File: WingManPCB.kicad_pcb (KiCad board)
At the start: 2 copper layers, 32 parts, among them SW1 SW_Push, U1 ATmega32U4-AU, Y1 Crystal_GND24_Small

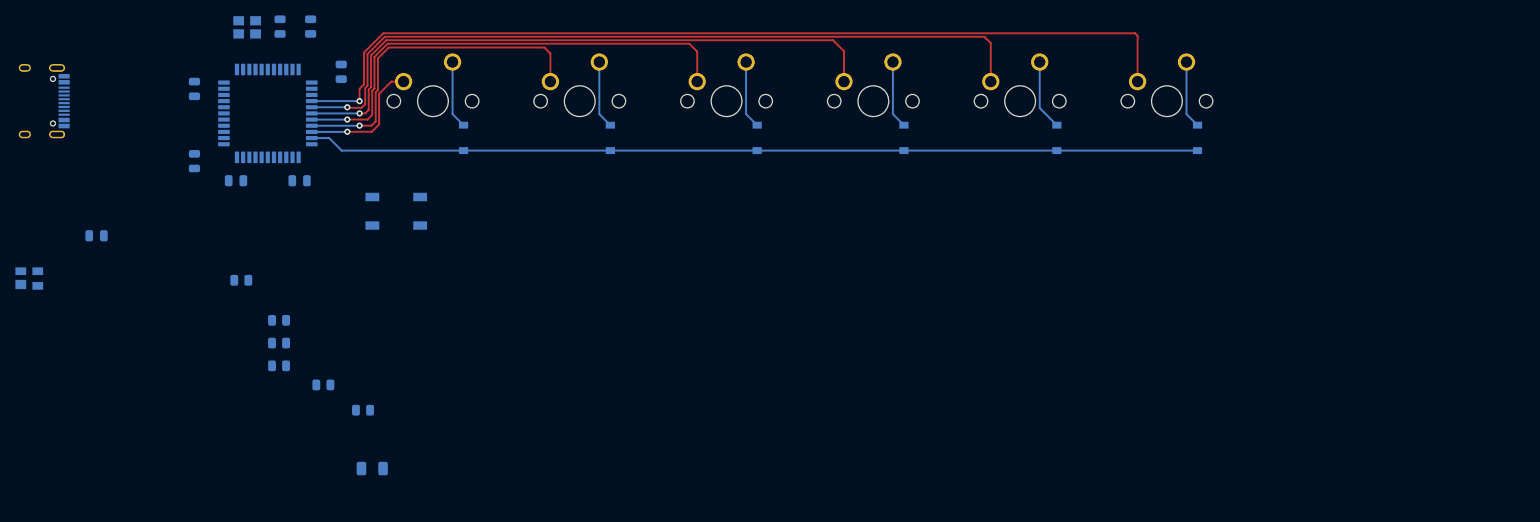
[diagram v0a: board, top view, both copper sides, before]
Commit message: PCB Outline Added
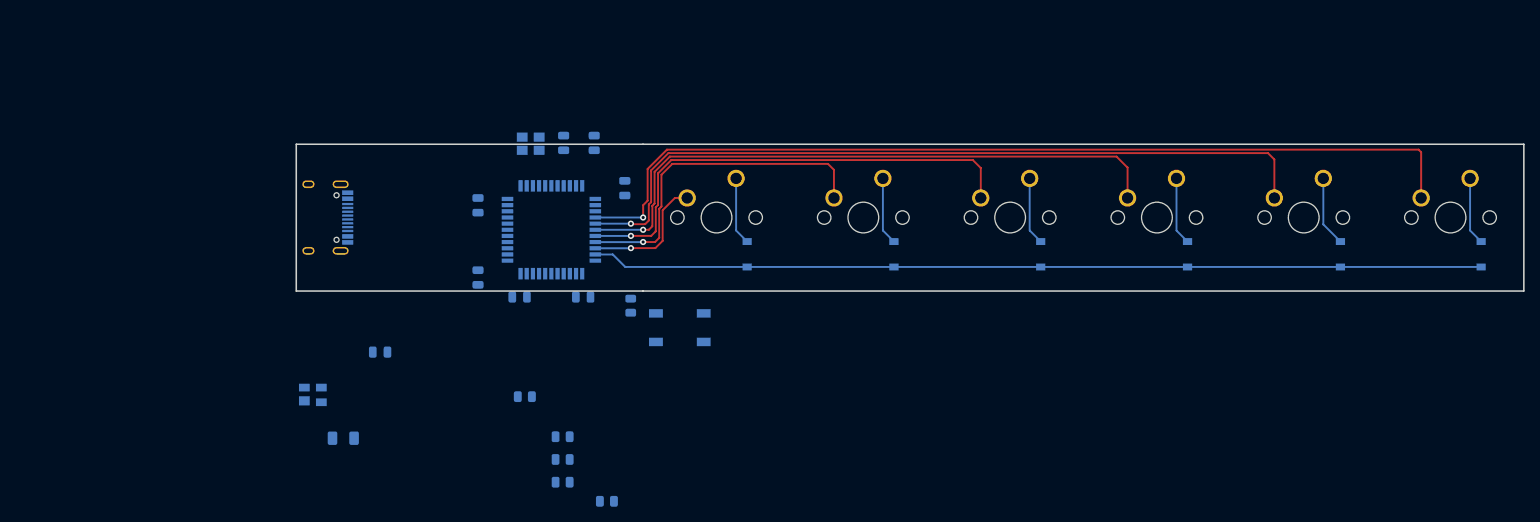
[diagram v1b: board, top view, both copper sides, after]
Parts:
- moved C3 39.8 mm to (102.7, 103.8)
- moved C7 39.8 mm to (102.7, 94.5)
- moved D4 39.8 mm to (175.7, 100.8)
- moved MX3 39.8 mm to (171.7, 96.1)
- moved MX5 39.8 mm to (209.8, 96.1)
- moved C1 39.8 mm to (90.0, 113.5)
- moved D3 39.8 mm to (156.7, 100.8)
- moved R4 39.8 mm to (108.8, 119.3)
- moved U1 39.8 mm to (112.2, 97.7)
- moved USB1 39.8 mm to (78.1, 96.1)
- moved Y1 39.8 mm to (109.5, 86.5)
- moved C2 39.8 mm to (113.8, 86.4)
- moved C4 39.8 mm to (108.1, 106.4)
- moved C5 39.8 mm to (116.3, 106.4)
- moved C6 39.8 mm to (121.7, 92.2)
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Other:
- board outline added: 159.3 x 19.1 mm
